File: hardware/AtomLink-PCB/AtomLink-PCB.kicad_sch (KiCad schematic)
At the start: 12 parts, among them Q1 AS2309, Q2 MUN5235

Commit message: Schematic changes & layout started
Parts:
- removed U?: LMZM23600, Package_LGA:Texas_SIL0010A_MicroSiP-10-1EP_3.8x3mm_P0.6mm_EP0.7x2.9mm_ThermalVias, symbol Regulator_Switching:LMZM23600
- added C1: 10u, Capacitor_SMD:C_1206_3216Metric, symbol Device:C
- added C2, C3: 10u, Capacitor_SMD:C_0805_2012Metric, symbol Device:C
- added D?: (no value), symbol Device:D
- added FID1: M2 hole, MountingHole:MountingHole_2.2mm_M2, symbol Mechanical:Fiducial
- added J1: Conn_01x03, Connector_PinHeader_2.54mm:PinHeader_1x03_P2.54mm_Horizontal, symbol Connector_Generic:Conn_01x03
- added J4: PF cable, Connector_PinHeader_1.27mm:PinHeader_1x04_P1.27mm_Vertical, symbol Connector_Generic:Conn_01x04
- added R4: 12k, Resistor_SMD:R_0402_1005Metric, symbol Device:R
- added R5: 0, Resistor_SMD:R_0402_1005Metric, symbol Device:R
- added R6: DNP, Resistor_SMD:R_0402_1005Metric, symbol Device:R
- added R8: 3.3k, Resistor_SMD:R_0402_1005Metric, symbol Device:R
- added R?: (no value), Resistor_SMD:R_0402_1005Metric, symbol Device:R
- added U1: LMZM23600V5, Package_LGA:Texas_SIL0010A_MicroSiP-10-1EP_3.8x3mm_P0.6mm_EP0.7x2.9mm_ThermalVias, symbol Regulator_Switching:LMZM23600V5
- D1: renamed from D?; value (none) -> PSM712; footprint (none) -> Package_TO_SOT_SMD:SOT-23
- J2: renamed from J?; value (none) -> Atom1; footprint (none) -> Connector_PinHeader_2.54mm:PinHeader_1x04_P2.54mm_Vertical
- J3: renamed from J?; value (none) -> Atom2; footprint (none) -> Connector_PinHeader_2.54mm:PinHeader_1x05_P2.54mm_Vertical
- Q1: footprint Package_TO_SOT_SMD:SOT-23_Handsoldering -> Package_TO_SOT_SMD:SOT-23
- Q2: footprint Package_TO_SOT_SMD:SOT-23_Handsoldering -> Package_TO_SOT_SMD:SOT-323_SC-70
- Q3: renamed from Q?; footprint Package_TO_SOT_SMD:SOT-23_Handsoldering -> Package_TO_SOT_SMD:SOT-23
- Q4: renamed from Q?; footprint Package_TO_SOT_SMD:SOT-23_Handsoldering -> Package_TO_SOT_SMD:SOT-323_SC-70
- R1: footprint Resistor_SMD:R_0603_1608Metric_Pad0.98x0.95mm_HandSolder -> Resistor_SMD:R_0805_2012Metric
- R2, R3: footprint Resistor_SMD:R_0603_1608Metric_Pad0.98x0.95mm_HandSolder -> Resistor_SMD:R_0402_1005Metric
- R7: renamed from R?; footprint Resistor_SMD:R_0603_1608Metric_Pad0.98x0.95mm_HandSolder -> Resistor_SMD:R_0805_2012Metric
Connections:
- net +5V: now also C2.1, C3.1, J1.2 (Pin_2), U1.6 (VOUT), U1.7 (FB)
- net G23: now also Q2.3 (C)
- net G33: now also Q4.3 (C)
- net GND: now also C1.2, C2.2, C3.2, J1.3 (Pin_3), J4.4 (Pin_4), R6.2, R8.2, U1.1 (GND), U1.11 (GND), U1.2 (MODE/SYNC)
- net PF_M1: now also D1.1 (A1), Q3.3 (D), J4.3 (Pin_3); no longer D1.2 (A2), Q3.2 (S)
- net PF_M2: now also D1.2 (A2), Q1.3 (D), J4.2 (Pin_2); no longer D1.1 (A1), Q1.2 (S)
- net VBUS: now also C1.1, J4.1 (Pin_1), R4.1, R5.1, U1.3 (VIN)
- net at Q2.1 (B): now also Q1.2 (S); no longer Q1.3 (D)
- net at Q4.1 (B): now also Q3.2 (S); no longer Q3.3 (D)
- net G25 renamed G25_ADC
- net G25_ADC: now also R4.2, R8.1
- removed net PF_IN1: Q2.3 (C), Q4.3 (C)
- new net: R5.2, R6.1, U1.4 (EN)
- new net: D?.1 (K), J1.1 (Pin_1)
- new net: D?.2 (A), R?.2
- no-connect marks 0 -> 1
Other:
- moved on the sheet: D1, J2, J3, Q1, Q2, Q3, Q4, R1, R2, R3, R7

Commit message: Schematic & layout changes
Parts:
- removed D?: (no value), symbol Device:D
- added D2: PSM712, Package_TO_SOT_SMD:SOT-23, symbol Diode:SM712_SOT23
- added D3: ?, symbol Device:D_Filled
- added Q5: MUN5235, Package_TO_SOT_SMD:SOT-323_SC-70, symbol Transistor_BJT:DTC123J
- added R10: ?, Resistor_SMD:R_0402_1005Metric, symbol Device:R
- F1: renamed from FID1; value M2 hole -> (none)
- R9: renamed from R?; value (none) -> 100
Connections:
- net +5V: now also R10.1
- net G19: now also Q5.1 (B)
- net G21: now also Q4.3 (C)
- net G22: now also D3.2 (A)
- net G23: no longer Q2.3 (C)
- net GND: now also D2.3 (common), Q5.2 (E)
- net VBUS: now also D2.1 (A1), D2.2 (A2)
- net at J1.1 (Pin_1): now also R9.2
- net at R9.1: now also D3.1 (K), Q5.3 (C), R10.2
- net G25_ADC renamed G33_ADC
- net G33_ADC: now also J3.1 (Pin_1); no longer J2.3 (Pin_3)
- removed net G33: J3.1 (Pin_1), Q4.3 (C)
- new net G25: J2.3 (Pin_3), Q2.3 (C)
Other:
- note added: "Standard pinout: G21 - M1 (IN) G25 - M2 (IN) G33 - VIN (IN, ADC) G19 - PWM TX (OUT) G22 - PWM RX (IN) Echo modified pinout: G21 - M1 (IN) G25 - M2 (IN) G26 - PWM TX (OUT) G32 - PWM RX (IN)"
- moved on the sheet: C1, C2, C3, D1, F1, J1, J2, J3, J4, Q1, Q2, Q3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

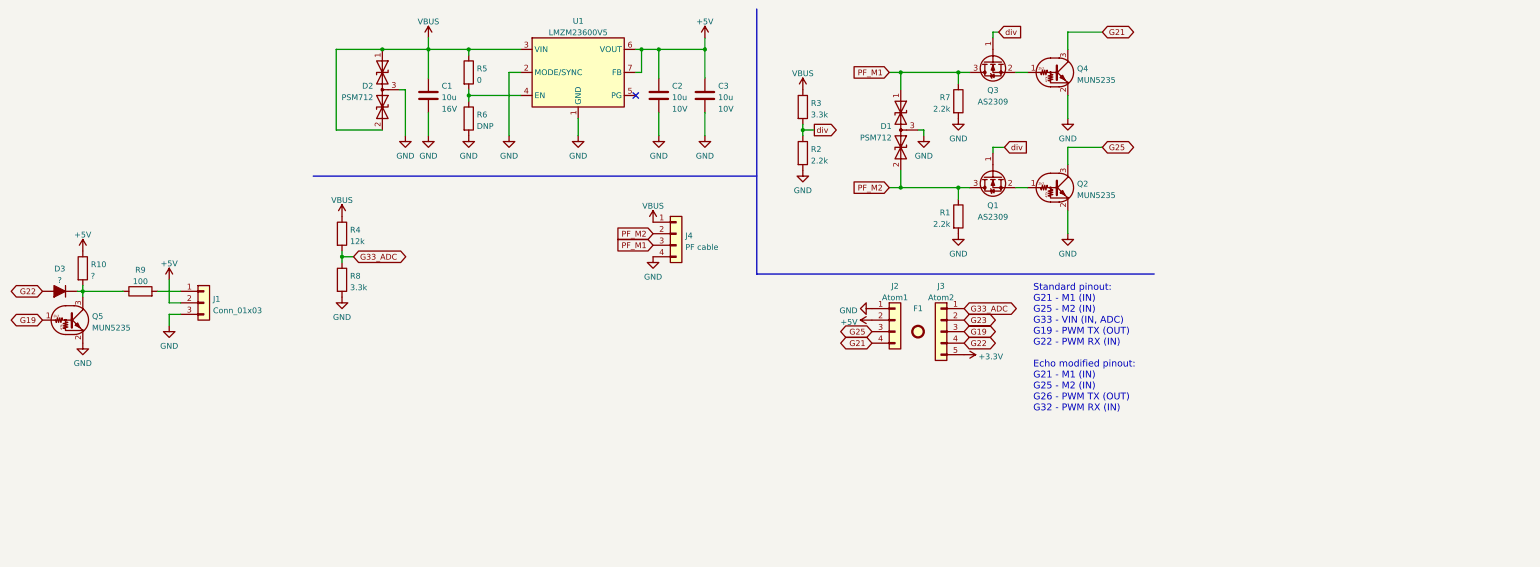
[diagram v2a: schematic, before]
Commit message: Added Echo variant
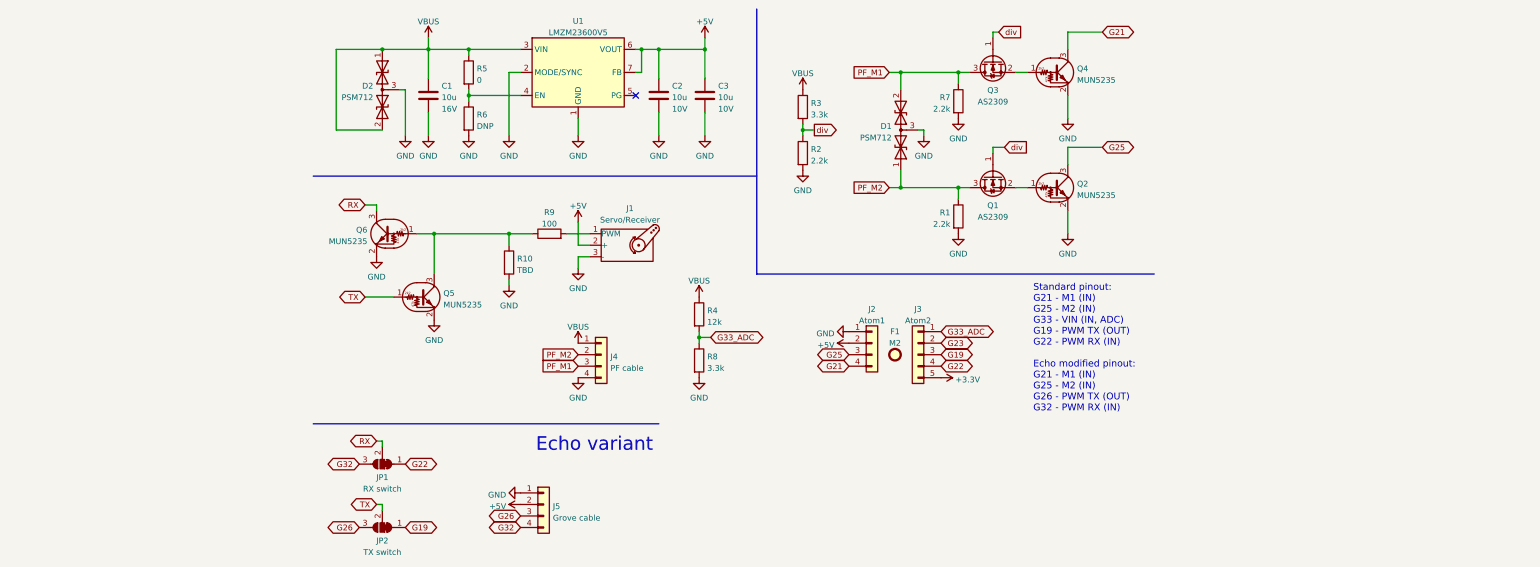
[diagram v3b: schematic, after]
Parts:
- removed D3: ?, symbol Device:D_Filled
- removed J1: Conn_01x03, Connector_PinHeader_2.54mm:PinHeader_1x03_P2.54mm_Horizontal, symbol Connector_Generic:Conn_01x03
- added J1: Servo/Receiver, Connector_PinHeader_2.54mm:PinHeader_1x03_P2.54mm_Horizontal, symbol Motor:Motor_Servo_Hitec
- added J5: Grove cable, AtomLink-footprints:PinHeader_1x04_2mm, symbol Connector_Generic:Conn_01x04
- added JP1: RX switch, Jumper:SolderJumper-3_P1.3mm_Bridged12_RoundedPad1.0x1.5mm, symbol Jumper:SolderJumper_3_Bridged12
- added JP2: TX switch, Jumper:SolderJumper-3_P1.3mm_Bridged12_RoundedPad1.0x1.5mm, symbol Jumper:SolderJumper_3_Bridged12
- added Q6: MUN5235, Package_TO_SOT_SMD:SOT-323_SC-70, symbol Transistor_BJT:DTC123J
- F1: value (none) -> M2
- J4: footprint Connector_PinHeader_1.27mm:PinHeader_1x04_P1.27mm_Vertical -> AtomLink-footprints:PinHeader_1x04_2mm
- R10: value ? -> TBD
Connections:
- net +5V: now also J1.2 (+), J5.2 (Pin_2); no longer R10.1
- net G19: now also JP2.1 (A); no longer Q5.1 (B)
- net G22: now also JP1.1 (A)
- net GND: now also R10.2, J1.3 (-), J5.1 (Pin_1), Q6.2 (E)
- net PF_M1: now also D1.2 (A2); no longer D1.1 (A1)
- net PF_M2: now also D1.1 (A1); no longer D1.2 (A2)
- net at Q5.3 (C), R9.1: now also R10.1, Q6.1 (B); no longer R10.2
- net at R9.2: now also J1.1 (PWM)
- new net G26: J5.3 (Pin_3), JP2.3 (B)
- new net G32: J5.4 (Pin_4), JP1.3 (B)
- new net RX: JP1.2 (C), Q6.3 (C)
- new net TX: JP2.2 (C), Q5.1 (B)
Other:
- note added: "Echo variant"
- company: (none) -> Aleksander Spyra
- title: (none) -> AtomLink
- moved on the sheet: F1, J2, J3, J4, Q5, R10, R4, R8, R9
